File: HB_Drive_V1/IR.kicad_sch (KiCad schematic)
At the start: 0 parts

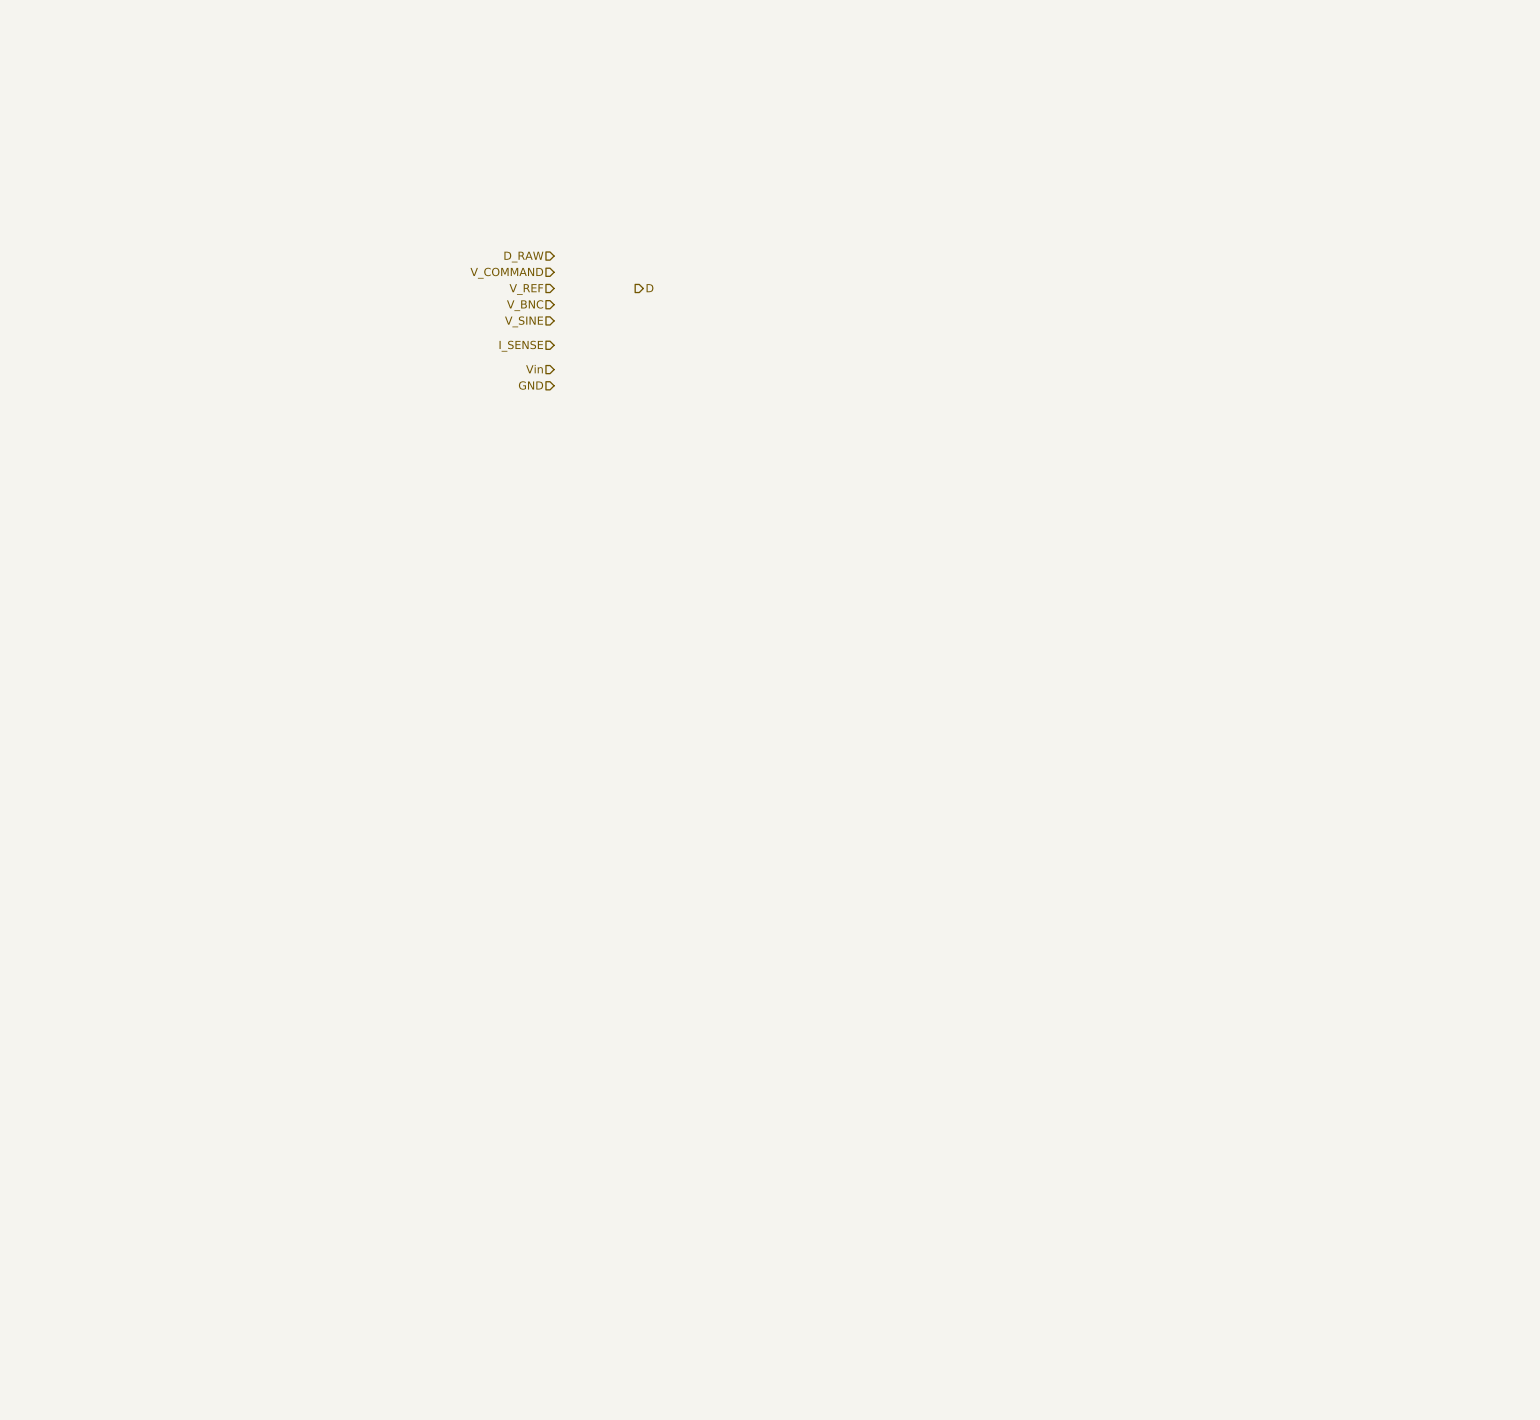
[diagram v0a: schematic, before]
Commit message: fixes git and adds a first revision of the Inner Current Regulator (NOT COMPLETE)
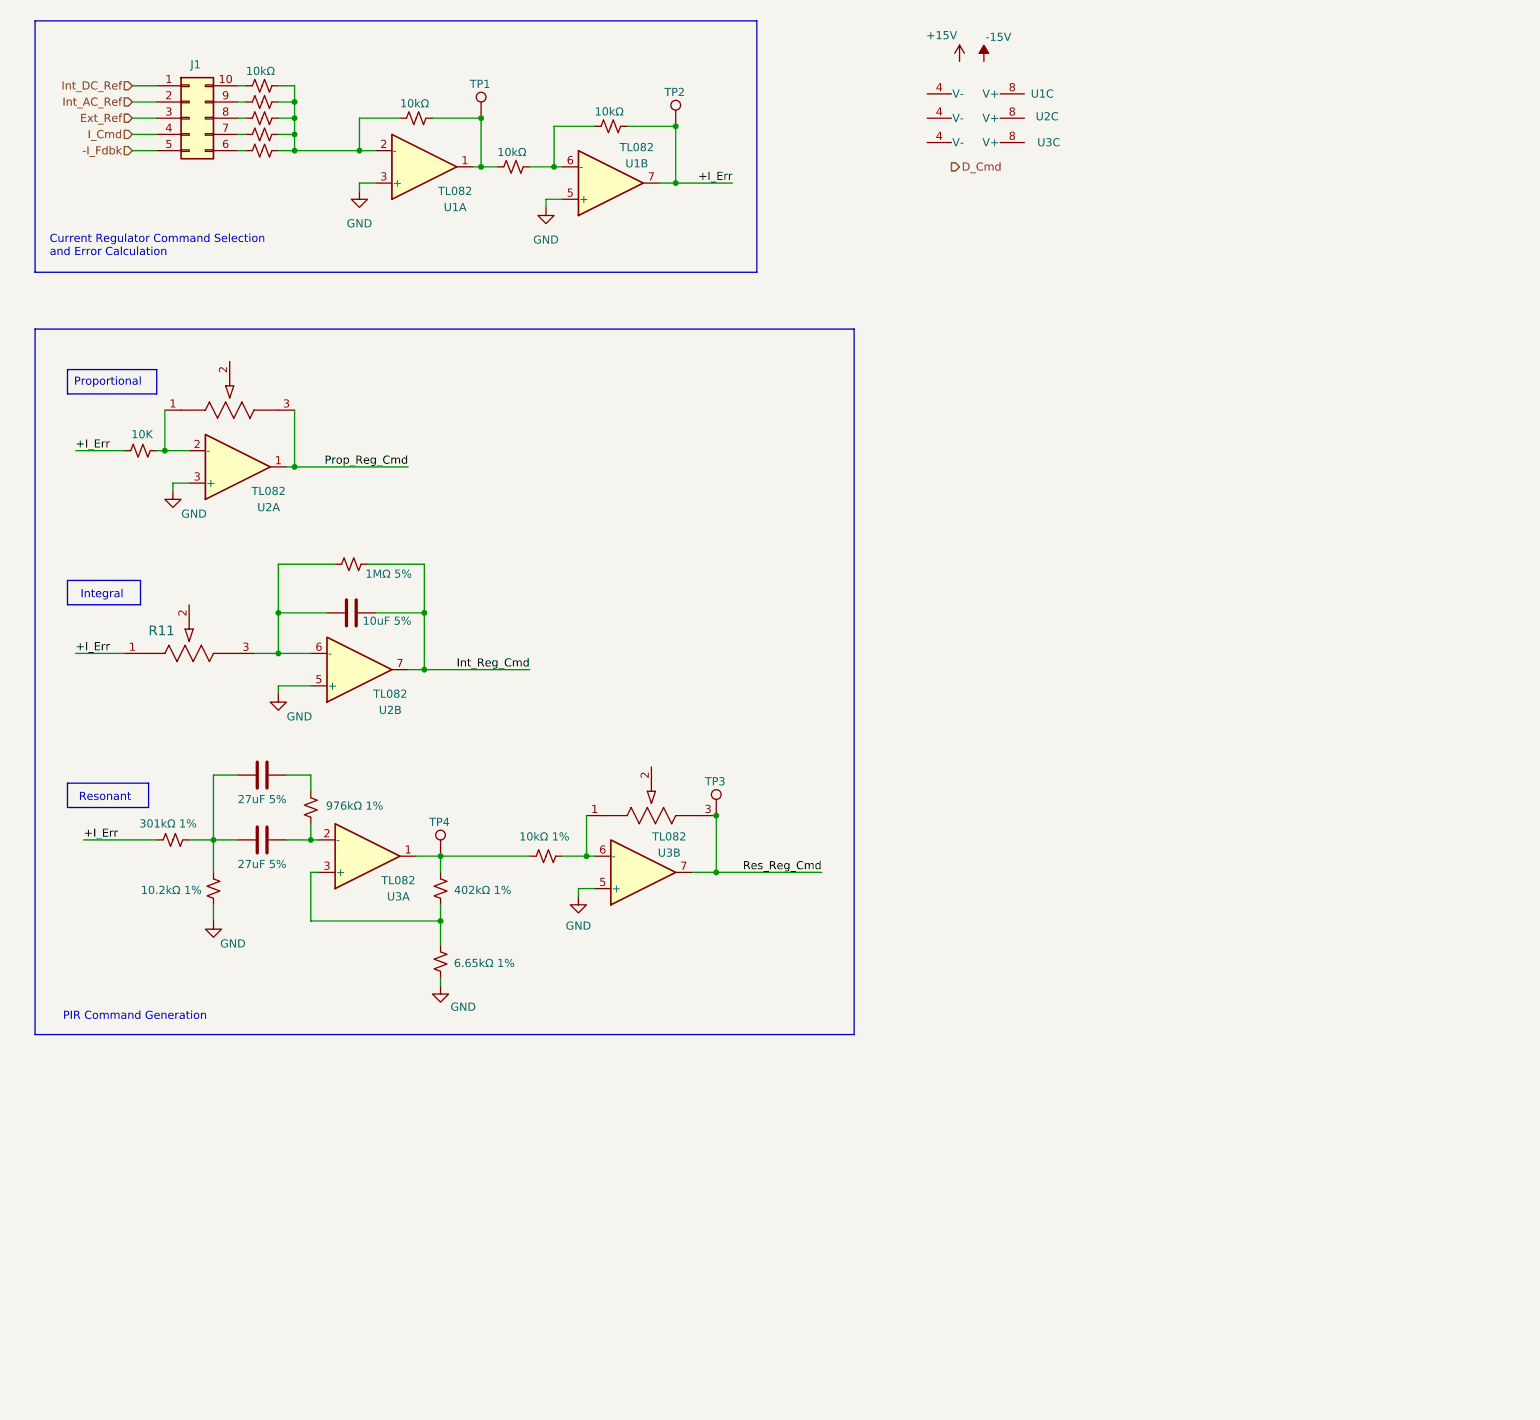
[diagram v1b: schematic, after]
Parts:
- added C1: 10uF 5%, Capacitor_SMD:C_0603_1608Metric, symbol Device:C
- added C2, C3: 27uF 5%, Capacitor_SMD:C_0603_1608Metric, symbol Device:C
- added J1: Conn_02x05_Counter_Clockwise, Connector_PinHeader_1.27mm:PinHeader_2x05_P1.27mm_Vertical, symbol Connector_Generic:Conn_02x05_Counter_Clockwise
- added R10, R11, R19: PV36W104C01B00, PV36W104C01B00:POT_PV36W_BRN, symbol PV36W104C01B00:PV36W104C01B00
- added R12: 1MΩ 5%, Resistor_SMD:R_0603_1608Metric_Pad0.98x0.95mm_HandSolder, symbol Device:R_Small_US
- added R13: 976kΩ 1%, Resistor_SMD:R_0603_1608Metric_Pad0.98x0.95mm_HandSolder, symbol Device:R_Small_US
- added R14: 301kΩ 1%, Resistor_SMD:R_0603_1608Metric_Pad0.98x0.95mm_HandSolder, symbol Device:R_Small_US
- added R15: 10.2kΩ 1%, Resistor_SMD:R_0603_1608Metric_Pad0.98x0.95mm_HandSolder, symbol Device:R_Small_US
- added R16: 402kΩ 1%, Resistor_SMD:R_0603_1608Metric_Pad0.98x0.95mm_HandSolder, symbol Device:R_Small_US
- added R17: 6.65kΩ 1%, Resistor_SMD:R_0603_1608Metric_Pad0.98x0.95mm_HandSolder, symbol Device:R_Small_US
- added R18: 10kΩ 1%, Resistor_SMD:R_0603_1608Metric_Pad0.98x0.95mm_HandSolder, symbol Device:R_Small_US
- added R2, R3, R4, R5, R9: 10K, Resistor_SMD:R_0603_1608Metric_Pad0.98x0.95mm_HandSolder, symbol Device:R_Small_US
- added R20, R21, R22, R23: 10kΩ, Resistor_SMD:R_0603_1608Metric_Pad0.98x0.95mm_HandSolder, symbol Device:R_Small_US
- added TP1, TP2, TP3, TP4: TestPoint, TestPoint:TestPoint_Loop_D2.60mm_Drill1.6mm_Beaded, symbol Connector:TestPoint
- added U1, U3: TL082, symbol Amplifier_Operational:TL082
- added U2: TL082, Package_SO:SOIC-8_5.3x5.3mm_P1.27mm, symbol Amplifier_Operational:TL082
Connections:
- net GND: now also R15.2, R17.1, U1.3 (+), U1.5 (+), U2.3 (+), U2.5 (+), U3.5 (+)
- new net: R22.1, R23.2, U1.6 (-)
- new net: C1.2, R11.3, R12.1, U2.6 (-)
- new net: R21.1, R22.2, TP1.1, U1.1
- new net: R10.1, R9.2, U2.2 (-)
- new net: J1.10 (Pin_10), R20.2
- new net: J1.6 (Pin_6), R5.1
- new net: J1.7 (Pin_7), R4.1
- new net: J1.8 (Pin_8), R3.1
- new net: J1.9 (Pin_9), R2.1
- new net: R16.2, R18.2, TP4.1, U3.1
- new net: C3.1, R13.1, U3.2 (-)
- new net: R16.1, R17.2, U3.3 (+)
- new net: C2.1, R13.2
- new net: C2.2, C3.2, R14.1, R15.1
- new net: R2.2, R20.1, R21.2, R3.2, R4.2, R5.2, U1.2 (-)
- new net: R18.1, R19.1, U3.6 (-)
- new net +I_Err: R11.1, R14.2, R23.1, R9.1, TP2.1, U1.7
- new net -I_Fdbk: J1.5 (Pin_5)
- new net Ext_Ref: J1.3 (Pin_3)
- new net I_Cmd: J1.4 (Pin_4)
- new net Int_AC_Ref: J1.2 (Pin_2)
- new net Int_DC_Ref: J1.1 (Pin_1)
- new net Int_Reg_Cmd: C1.1, R12.2, U2.7
- new net Prop_Reg_Cmd: R10.3, U2.1
- new net Res_Reg_Cmd: R19.3, TP3.1, U3.7
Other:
- note added: "Current Regulator Command Selection and Error Calculation"
- note added: "Integral"
- note added: "PIR Command Generation"
- note added: "Proportional"
- note added: "Resonant"

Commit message: Finishes first revision of the Inner Current Regulator!
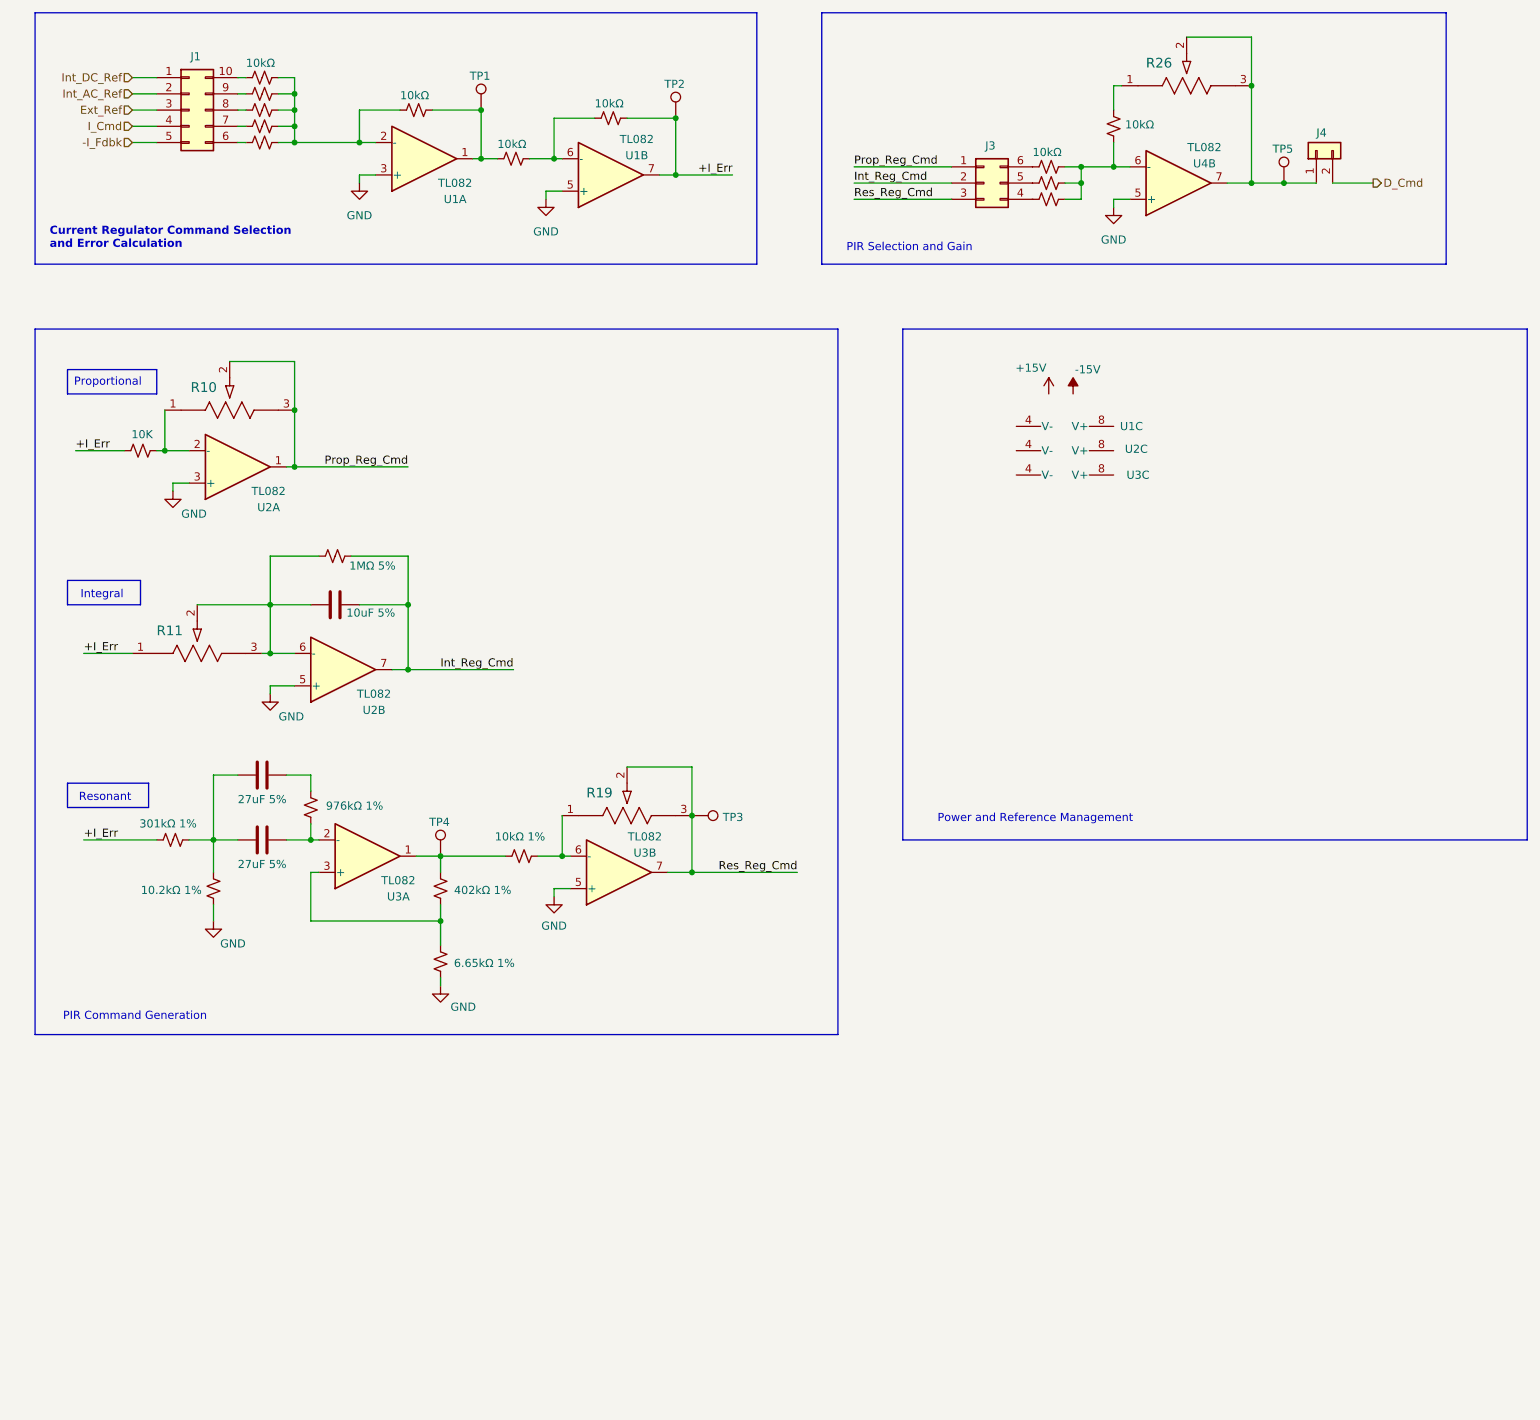
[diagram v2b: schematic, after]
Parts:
- added J3: Conn_02x03_Counter_Clockwise, Connector_PinSocket_1.27mm:PinSocket_2x03_P1.27mm_Vertical, symbol Connector_Generic:Conn_02x03_Counter_Clockwise
- added J4: Conn_01x02, symbol Connector_Generic:Conn_01x02
- added R24, R25: 10kΩ, Resistor_SMD:R_0603_1608Metric_Pad0.98x0.95mm_HandSolder, symbol Device:R_Small_US
- added R26: PV36W104C01B00, PV36W104C01B00:POT_PV36W_BRN, symbol PV36W104C01B00:PV36W104C01B00
- added R6, R7: 10K, Resistor_SMD:R_0603_1608Metric_Pad0.98x0.95mm_HandSolder, symbol Device:R_Small_US
- added TP5: TestPoint, TestPoint:TestPoint_Loop_D2.60mm_Drill1.6mm_Beaded, symbol Connector:TestPoint
- added U4: TL082, symbol Amplifier_Operational:TL082
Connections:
- net D_Cmd: now also J4.2 (Pin_2)
- net GND: now also U4.5 (+)
- net Int_Reg_Cmd: now also J3.2 (Pin_2)
- net Prop_Reg_Cmd: now also R10.2, J3.1 (Pin_1)
- net Res_Reg_Cmd: now also R19.2, J3.3 (Pin_3)
- net at C1.2, R11.3, R12.1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: now also R11.2
- new net: J3.4 (Pin_4), R7.1
- new net: J3.5 (Pin_5), R6.1
- new net: J3.6 (Pin_6), R24.2
- new net: R24.1, R25.1, R6.2, R7.2, U4.6 (-)
- new net: J4.1 (Pin_1), R26.2, R26.3, TP5.1, U4.7
- new net: R25.2, R26.1
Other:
- note added: "PIR Selection and Gain"
- note added: "Power and Reference Management"
- moved on the sheet: J1, R11, TP1, TP2, TP3, U1A, U1B, U1C, U2B, U2C, U3B, U3C
